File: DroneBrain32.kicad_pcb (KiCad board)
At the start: 2 copper layers, 49 x 27.5 mm, 45 parts, among them J1 HEADER1X2, J10 HEADER1X10, J11 GSM, J2 AIN0, J3 JTAG, J4 AIN1, J5 GPS, J6 USB-MINI-A, J7 IMU, J8 HEADER1X10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

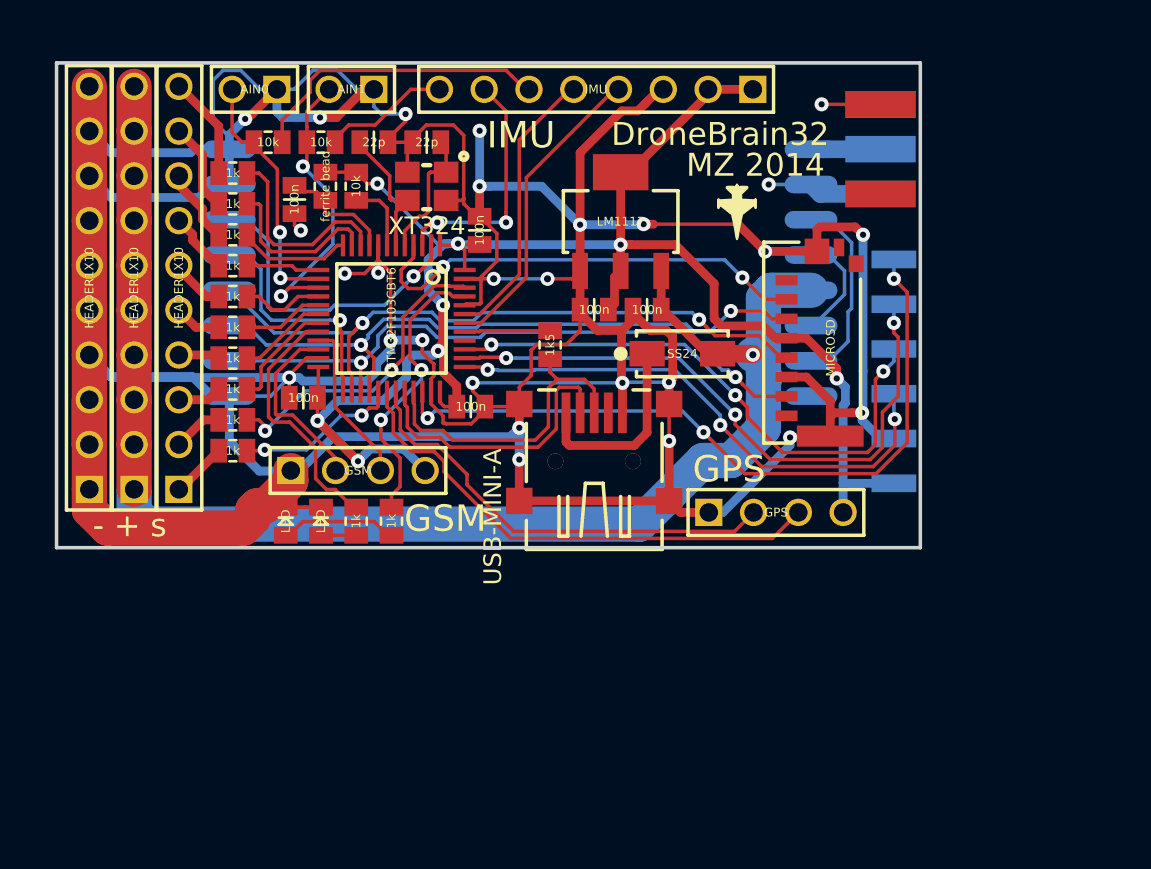
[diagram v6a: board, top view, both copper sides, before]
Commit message: Improved GND
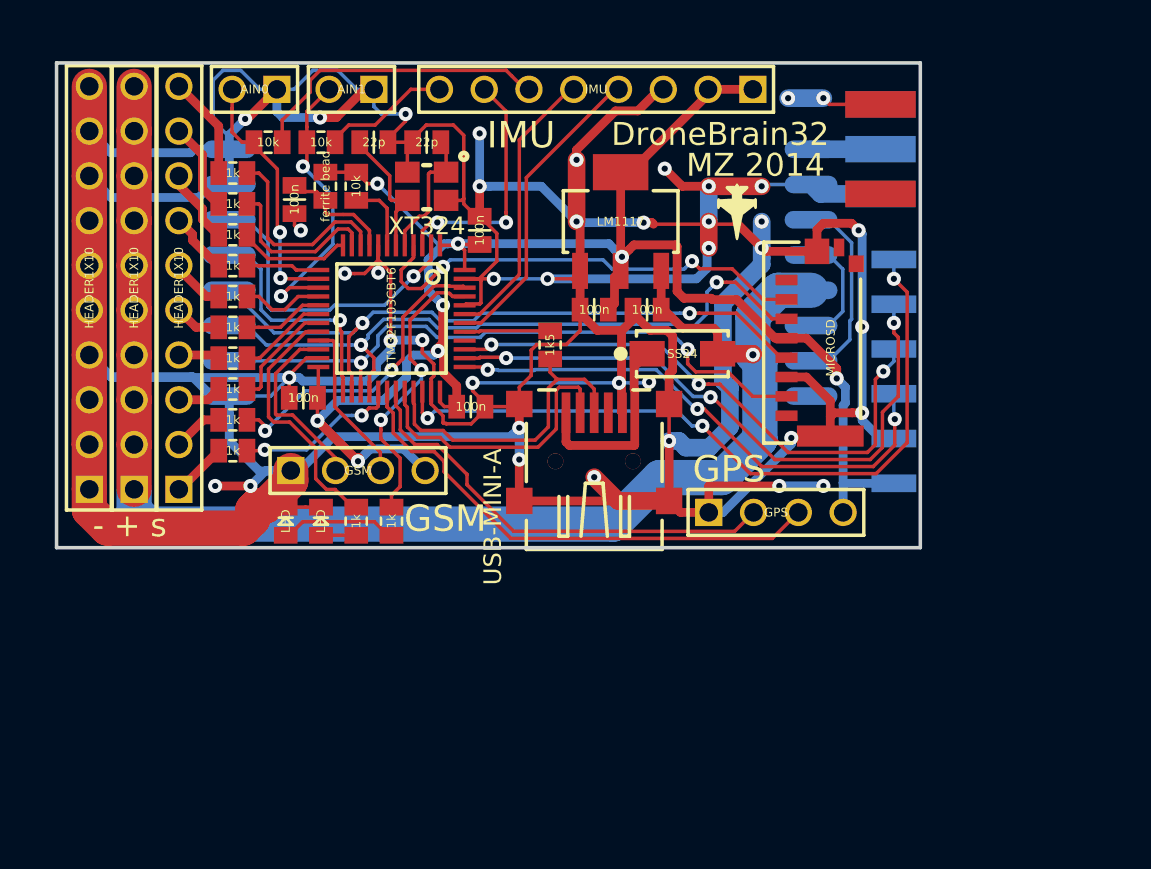
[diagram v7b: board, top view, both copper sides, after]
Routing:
- net GND: track 344.6 -> 400.5 mm, vias 27 -> 40
- net /MOSI: track 37.0 -> 38.8 mm
- net +3V3: track 106.4 -> 107.3 mm
